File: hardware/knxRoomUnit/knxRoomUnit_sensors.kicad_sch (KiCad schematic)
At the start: 13 parts, among them U2 BME280, U3 VCNL4040M3OE

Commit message: Initial hardware commit
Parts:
- added R23: 8.2k, Resistor_SMD:R_0603_1608Metric, symbol Device:R
- added U4: SHT31-DIS, Sensor_Humidity:Sensirion_DFN-8-1EP_2.5x2.5mm_P0.5mm_EP1.1x1.7mm, symbol Sensor_Humidity:SHT31-DIS
- R19: renamed from R18; footprint Resistor_SMD:R_0402_1005Metric -> Resistor_SMD:R_0603_1608Metric
- R20: renamed from R19; footprint Resistor_SMD:R_0402_1005Metric -> Resistor_SMD:R_0603_1608Metric
- R21: renamed from R20; footprint Resistor_SMD:R_0402_1005Metric -> Resistor_SMD:R_0603_1608Metric
- R22: renamed from R21; footprint Resistor_SMD:R_0402_1005Metric -> Resistor_SMD:R_0603_1608Metric
- R24: renamed from R22; footprint Resistor_SMD:R_0402_1005Metric -> Resistor_SMD:R_0603_1608Metric
- R25: renamed from R23; footprint Resistor_SMD:R_0402_1005Metric -> Resistor_SMD:R_0603_1608Metric
- R26: renamed from R24; footprint Resistor_SMD:R_0402_1005Metric -> Resistor_SMD:R_0603_1608Metric
- U5: renamed from U3; footprint libs:VISHAY_VCNL4040_4X2X1.1 -> (none)
- renumbered U2 to U3
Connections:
- net at C17.1, C18.1, R22.2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: now also R23.1; no longer U5.3
- new net: R23.2, U5.3
- new net: U4.8 (VSS), U4.9 (VSS)
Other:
- moved on the sheet: C17, C18, R22

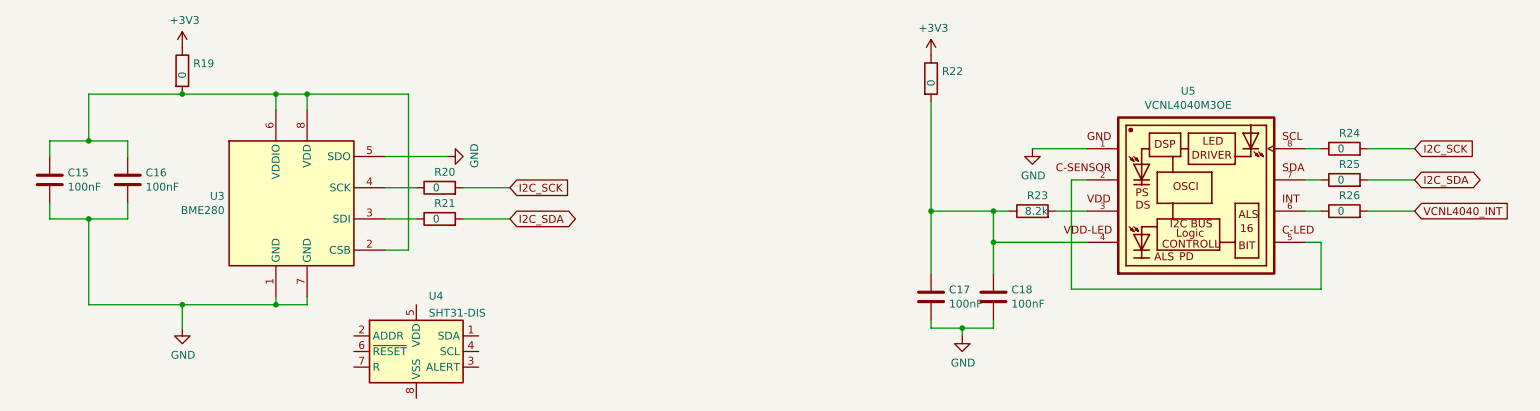
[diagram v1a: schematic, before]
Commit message: Updated sensors
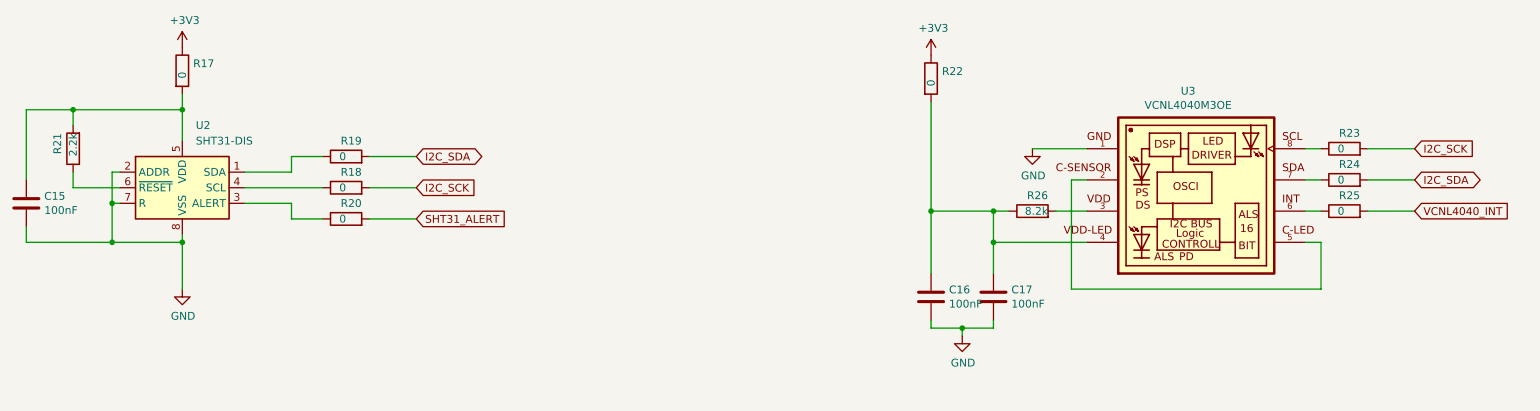
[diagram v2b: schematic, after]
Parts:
- removed C16: 100nF, Capacitor_SMD:C_0603_1608Metric, symbol Device:C
- removed U3: BME280, Package_LGA:Bosch_LGA-8_2.5x2.5mm_P0.65mm_ClockwisePinNumbering, symbol Sensor:BME280
- added R20: 0, Resistor_SMD:R_0603_1608Metric, symbol Device:R
- added R21: 2.2k, Resistor_SMD:R_0603_1608Metric, symbol Device:R
- U3: renamed from U5; footprint (none) -> VCNL4040M3OE:VISHAY_VCNL4040_4X2X1.1; Availability (none) -> In Stock; Check_prices (none) -> https://www.snapeda.com/parts/VCNL4040M3OE/Vishay+Semicondu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; MF (none) -> Vishay; MP (none) -> VCNL4040M3OE; Package (none) -> None; Price (none) -> None; Purchase-URL (none) -> https://pricing.snapeda.com/search?q=VCNL4040M3OE&ref=eda; SnapEDA_Link (none) -> https://www.snapeda.com/parts/VCNL4040M3OE/Vishay+Semicondu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
- renumbered C17 to C16, C18 to C17, R19 to R17, R20 to R18, R21 to R19, R24 to R23, R25 to R24, R26 to R25, R23 to R26, U4 to U2
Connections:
- net GND: now also U2.2 (ADDR), U2.7 (R), U2.8 (VSS), U2.9 (VSS)
- net at C15.1, R17.2: now also U2.5 (VDD), R21.2
- net at R19.1: now also U2.1 (SDA)
- net at R18.1: now also U2.4 (SCL)
- net at U2.3 (ALERT): now also R20.1
- net at U2.6 (~{RESET}): now also R21.1
- new net SHT31_ALERT: R20.2
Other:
- moved on the sheet: R18, R19, U2

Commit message: PCB routing
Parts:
- R17, R18, R19, R20, R22, R23, R24, R25: footprint Resistor_SMD:R_0603_1608Metric -> Resistor_SMD:R_0201_0603Metric
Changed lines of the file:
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@@
       (effects (font (size 1.27 1.27)) (justify left))
     )
-    (property "Footprint" "Resistor_SMD:R_0603_1608Metric" (at 40.132 27.94 90)
+    (property "Footprint" "Resistor_SMD:R_0201_0603Metric" (at 40.132 27.94 90)
       (effects (font (size 1.27 1.27)) hide)
     )
@@
       (effects (font (size 1.27 1.27)) (justify left))
     )
-    (property "Footprint" "Resistor_SMD:R_0603_1608Metric" (at 68.58 48.768 90)
+    (property "Footprint" "Resistor_SMD:R_0201_0603Metric" (at 68.58 48.768 90)
       (effects (font (size 1.27 1.27)) hide)
     )
@@
       (effects (font (size 1.27 1.27)) (justify left))
     )
-    (property "Footprint" "Resistor_SMD:R_0603_1608Metric" (at 68.58 43.688 90)
+    (property "Footprint" "Resistor_SMD:R_0201_0603Metric" (at 68.58 43.688 90)
       (effects (font (size 1.27 1.27)) hide)
     )
@@
       (effects (font (size 1.27 1.27)) (justify left))
     )
-    (property "Footprint" "Resistor_SMD:R_0603_1608Metric" (at 162.052 29.21 90)
+    (property "Footprint" "Resistor_SMD:R_0201_0603Metric" (at 162.052 29.21 90)
       (effects (font (size 1.27 1.27)) hide)
     )
@@
       (effects (font (size 1.27 1.27)) (justify left))
     )
-    (property "Footprint" "Resistor_SMD:R_0603_1608Metric" (at 231.14 42.418 90)
+    (property "Footprint" "Resistor_SMD:R_0201_0603Metric" (at 231.14 42.418 90)
       (effects (font (size 1.27 1.27)) hide)
     )
@@
       (effects (font (size 1.27 1.27)) (justify left))
     )
-    (property "Footprint" "Resistor_SMD:R_0603_1608Metric" (at 231.14 47.498 90)
+    (property "Footprint" "Resistor_SMD:R_0201_0603Metric" (at 231.14 47.498 90)
       (effects (font (size 1.27 1.27)) hide)
     )
@@
       (effects (font (size 1.27 1.27)) (justify left))
     )
-    (property "Footprint" "Resistor_SMD:R_0603_1608Metric" (at 231.14 52.578 90)
+    (property "Footprint" "Resistor_SMD:R_0201_0603Metric" (at 231.14 52.578 90)
       (effects (font (size 1.27 1.27)) hide)
     )
@@
       (effects (font (size 1.27 1.27)) (justify left))
     )
-    (property "Footprint" "Resistor_SMD:R_0603_1608Metric" (at 68.58 53.848 90)
-      (effects (font (size 1.27 1.27)) hide)
-    )
+    (property "Footprint" "Resistor_SMD:R_0201_0603Metric" (at 68.58 53.848 90)
+      (effects (font (size 1.27 1.27)) hide)
+    )

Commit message: Production adjustments
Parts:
- R17, R18, R19, R20, R22, R23, R24, R25: LCSC Part # C17168 -> C21189; Manufacturer Uniroyal Elec -> UNI-ROYAL(Uniroyal Elec); PartNumber 0402WGF0000TCE -> 0603WAF0000T5E
- R21: LCSC Part # C17168 -> C4190; Manufacturer Uniroyal Elec -> UNI-ROYAL(Uniroyal Elec); PartNumber 0402WGF0000TCE -> 0603WAF2201T5E
- R26: LCSC Part # C17168 -> C25981; Manufacturer Uniroyal Elec -> UNI-ROYAL(Uniroyal Elec); PartNumber 0402WGF0000TCE -> 0603WAF8201T5E
- U2: LCSC Part # (none) -> C80862; Manufacturer (none) -> Sensirion; PartNumber (none) -> SHT31-DIS-B2.5kS
- U3: MF Vishay -> (none); TAPE_REEL YES -> (none); VOLUME MOQ: 2500 pcs -> (none)

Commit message: Updated HW design
Flipped P1 to match display's pinout
Changed 0201 resistors to 0603
Added R12 to section 3V3 to display
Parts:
- R17, R18, R19, R20, R22, R23, R24, R25: footprint Resistor_SMD:R_0201_0603Metric -> Resistor_SMD:R_0603_1608Metric
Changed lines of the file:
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@@
   (title_block
     (title "knxRoomUnit")
-    (date "2023-08-22")
-    (rev "r1d0")
+    (date "2024-01-21")
+    (rev "r1d1")
     (company "MP")
   )
@@
       (effects (font (size 1.27 1.27)) (justify left))
     )
-    (property "Footprint" "Resistor_SMD:R_0201_0603Metric" (at 40.132 27.94 90)
+    (property "Footprint" "Resistor_SMD:R_0603_1608Metric" (at 40.132 27.94 90)
       (effects (font (size 1.27 1.27)) hide)
     )
@@
       (effects (font (size 1.27 1.27)) (justify left))
     )
-    (property "Footprint" "Resistor_SMD:R_0201_0603Metric" (at 68.58 48.768 90)
+    (property "Footprint" "Resistor_SMD:R_0603_1608Metric" (at 68.58 48.768 90)
       (effects (font (size 1.27 1.27)) hide)
     )
@@
       (effects (font (size 1.27 1.27)) (justify left))
     )
-    (property "Footprint" "Resistor_SMD:R_0201_0603Metric" (at 68.58 43.688 90)
+    (property "Footprint" "Resistor_SMD:R_0603_1608Metric" (at 68.58 43.688 90)
       (effects (font (size 1.27 1.27)) hide)
     )
@@
       (effects (font (size 1.27 1.27)) (justify left))
     )
-    (property "Footprint" "Resistor_SMD:R_0201_0603Metric" (at 162.052 29.21 90)
+    (property "Footprint" "Resistor_SMD:R_0603_1608Metric" (at 162.052 29.21 90)
       (effects (font (size 1.27 1.27)) hide)
     )
@@
       (effects (font (size 1.27 1.27)) (justify left))
     )
-    (property "Footprint" "Resistor_SMD:R_0201_0603Metric" (at 231.14 42.418 90)
+    (property "Footprint" "Resistor_SMD:R_0603_1608Metric" (at 231.14 42.418 90)
       (effects (font (size 1.27 1.27)) hide)
     )
@@
       (effects (font (size 1.27 1.27)) (justify left))
     )
-    (property "Footprint" "Resistor_SMD:R_0201_0603Metric" (at 231.14 47.498 90)
+    (property "Footprint" "Resistor_SMD:R_0603_1608Metric" (at 231.14 47.498 90)
       (effects (font (size 1.27 1.27)) hide)
     )
@@
       (effects (font (size 1.27 1.27)) (justify left))
     )
-    (property "Footprint" "Resistor_SMD:R_0201_0603Metric" (at 231.14 52.578 90)
+    (property "Footprint" "Resistor_SMD:R_0603_1608Metric" (at 231.14 52.578 90)
       (effects (font (size 1.27 1.27)) hide)
     )
@@
       (effects (font (size 1.27 1.27)) (justify left))
     )
-    (property "Footprint" "Resistor_SMD:R_0201_0603Metric" (at 68.58 53.848 90)
-      (effects (font (size 1.27 1.27)) hide)
-    )
+    (property "Footprint" "Resistor_SMD:R_0603_1608Metric" (at 68.58 53.848 90)
+      (effects (font (size 1.27 1.27)) hide)
+    )
